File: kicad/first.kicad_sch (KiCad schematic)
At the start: 22 parts, among them J1 Conn_01x04_Pin, P1 USB_C_Plug_USB2.0, SW1 SW_SPDT, U1 STM32F407VETx, Y1 X MHz

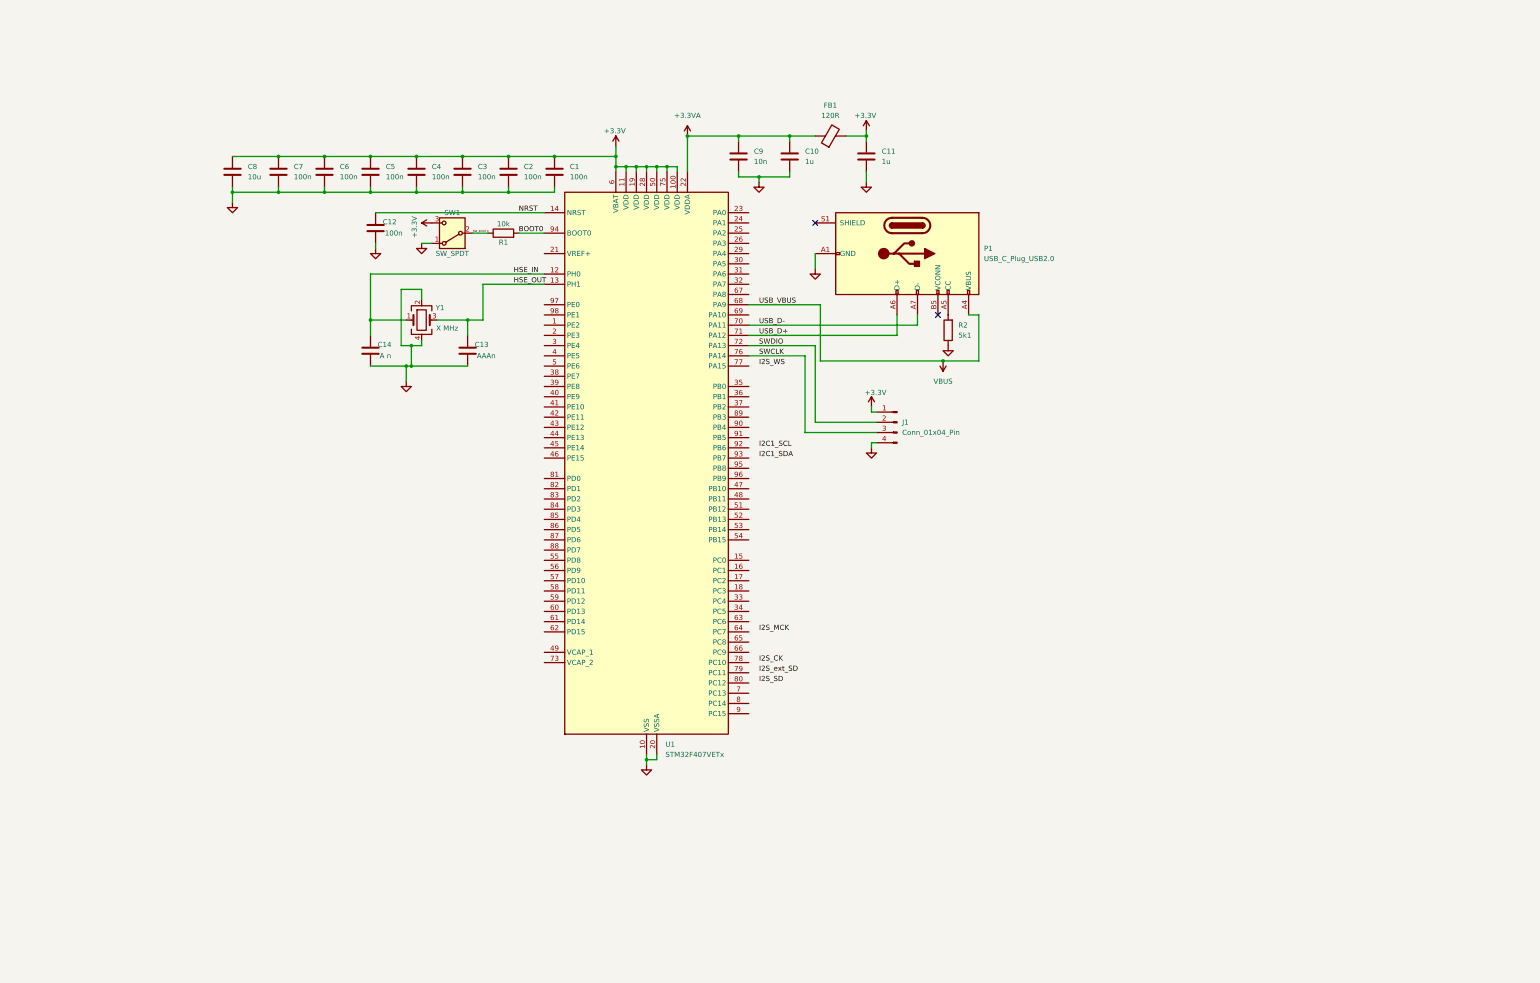
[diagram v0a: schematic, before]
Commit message: added LDO
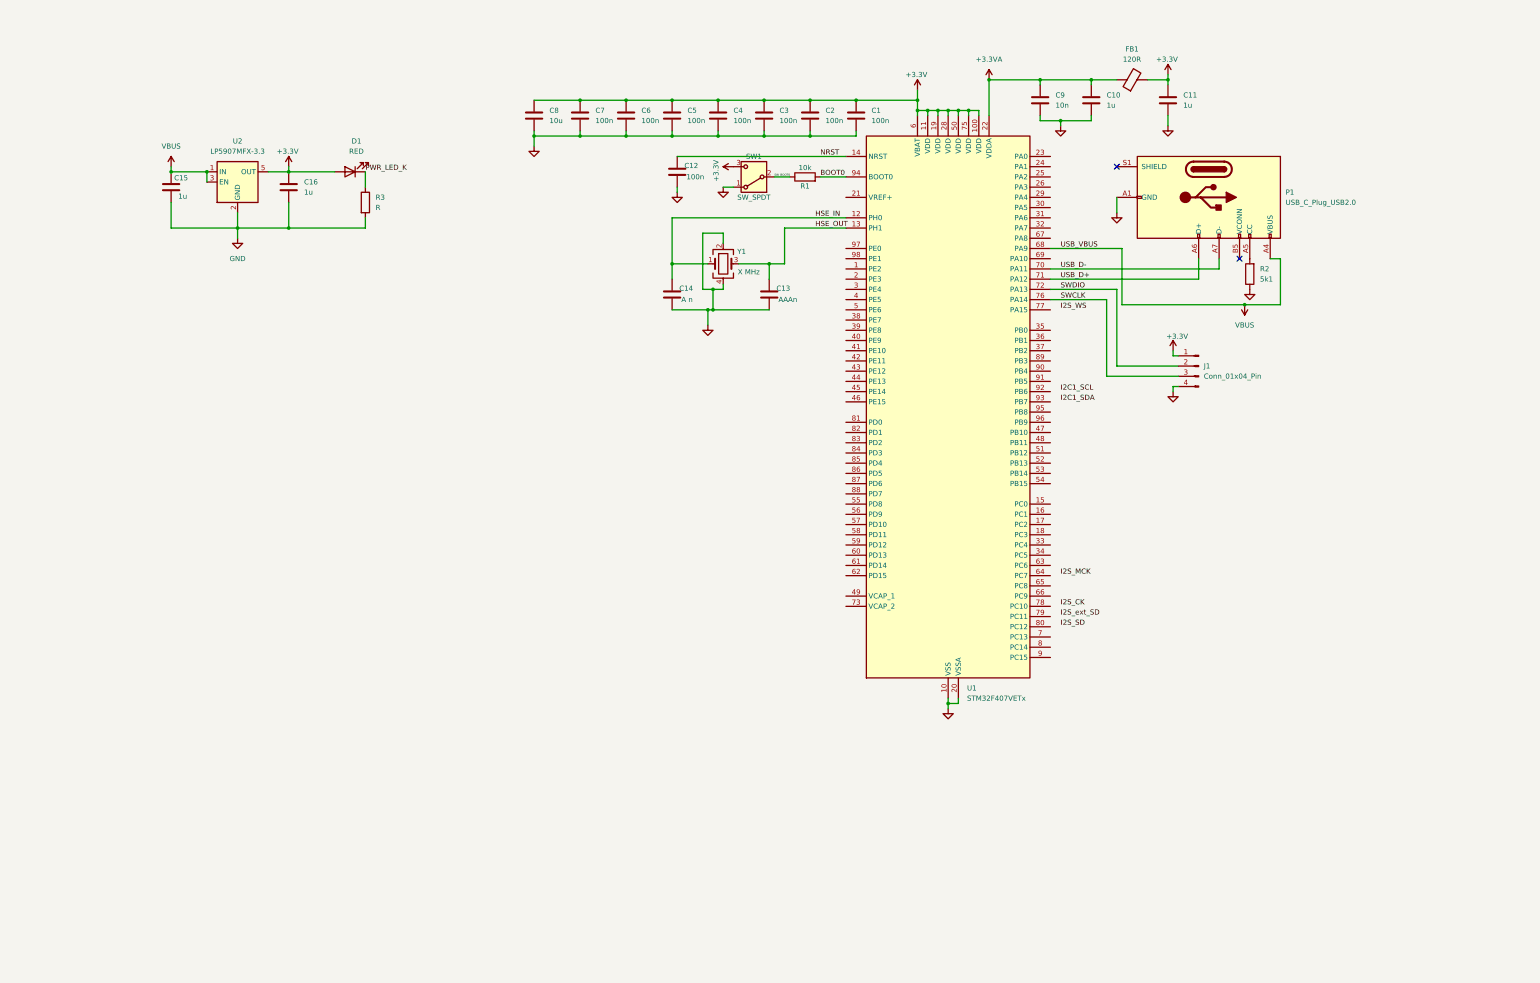
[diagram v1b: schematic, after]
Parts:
- added C15, C16: 1u, symbol Device:C
- added D1: RED, symbol Device:LED
- added R3: R, symbol Device:R
- added U2: LP5907MFX-3.3, Package_TO_SOT_SMD:SOT-23-5, symbol Regulator_Linear:LP5907MFX-3.3
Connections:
- net +3.3V: now also C16.1, D1.2 (A), U2.5 (OUT)
- net GND: now also C15.2, C16.2, R3.2, U2.2 (GND)
- net VBUS: now also C15.1, U2.1 (IN), U2.3 (EN)
- new net PWR_LED_K: D1.1 (K), R3.1
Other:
- moved on the sheet: C1, C10, C11, C12, C13, C14, C2, C3, C4, C5, C6, C7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

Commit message: audio codec + input audio buffers
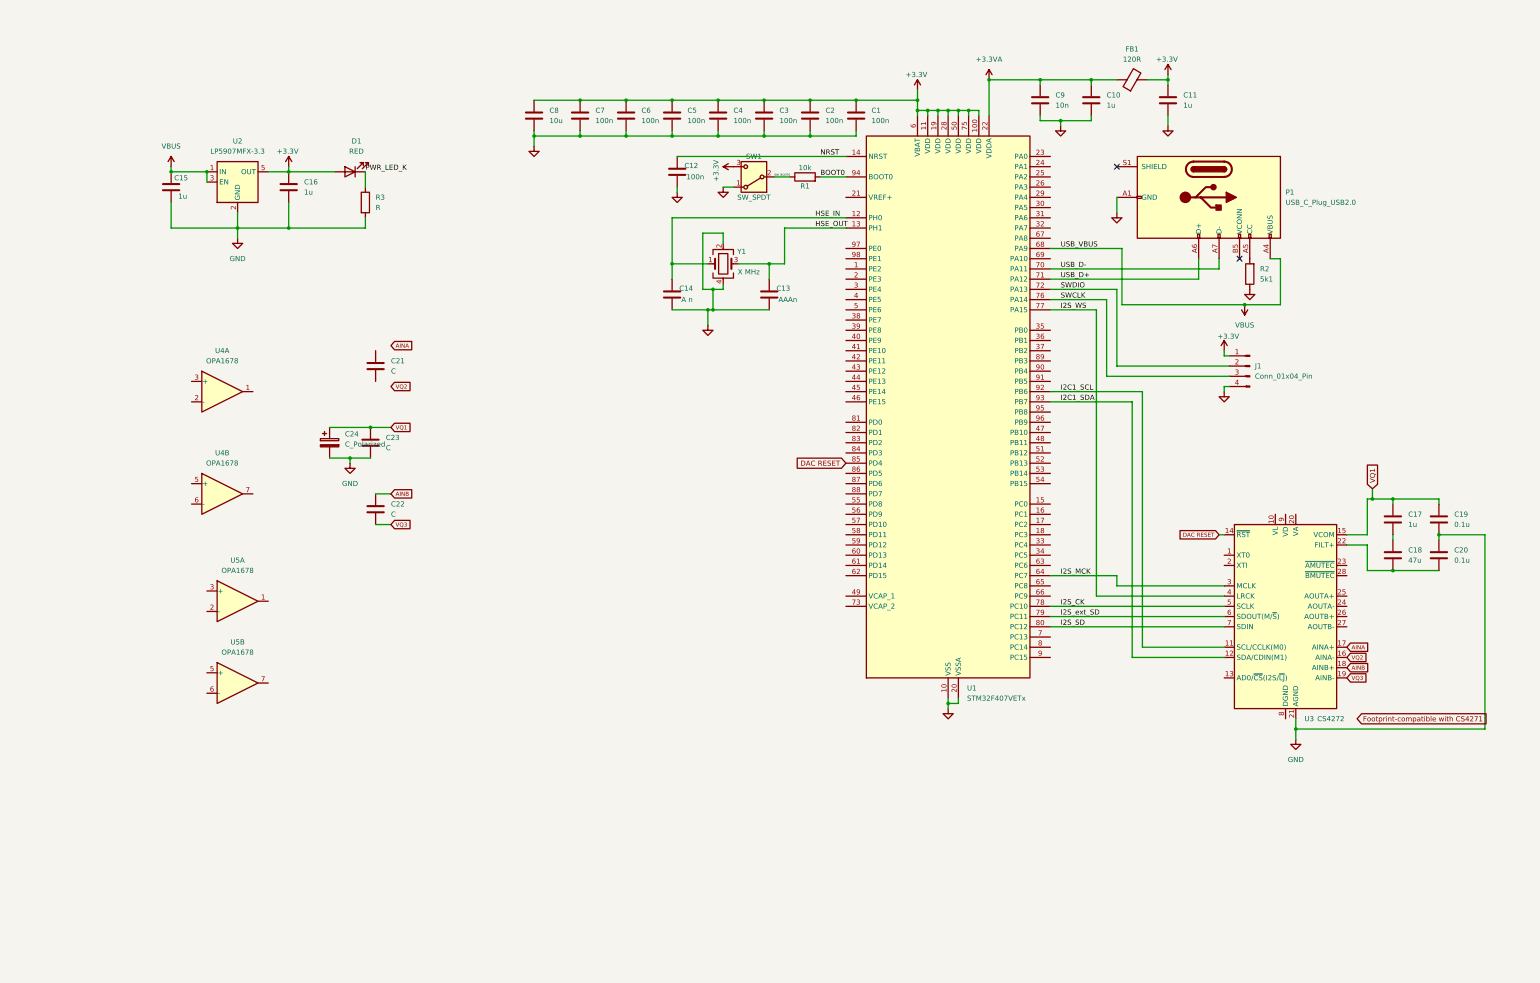
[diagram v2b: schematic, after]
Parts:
- added C17: 1u, symbol Device:C
- added C18: 47u, symbol Device:C
- added C19, C20: 0.1u, symbol Device:C
- added C21, C22, C23: C, symbol Device:C
- added C24: C_Polarized, symbol Device:C_Polarized
- added U3: CS4272, Package_SO:TSSOP-28_4.4x9.7mm_P0.65mm, symbol Audio:CS4272
- added U4, U5: OPA1678, Package_SO:SOIC-8_3.9x4.9mm_P1.27mm, symbol Amplifier_Operational:OPA1678
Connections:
- net GND: now also C19.2, C20.1, C23.2, C24.2, U3.21 (AGND)
- net I2C1_SCL: now also U1.92 (PB6), U3.11 (SCL/CCLK(M0))
- net I2C1_SDA: now also U1.93 (PB7), U3.12 (SDA/CDIN(M1))
- net I2S_CK: now also U1.78 (PC10), U3.5 (SCLK)
- net I2S_MCK: now also U1.64 (PC7), U3.3 (MCLK)
- net I2S_SD: now also U1.80 (PC12), U3.7 (SDIN)
- net I2S_WS: now also U1.77 (PA15), U3.4 (LRCK)
- net I2S_ext_SD: now also U1.79 (PC11), U3.6 (SDOUT(M/~{S}))
- net DAC RESET: now reaches U1.85 (PD4)
- net DAC RESET: now also U3.14 (~{RST})
- new net: C18.2, C20.2, U3.22 (FILT+)
- new net: C17.2, C18.1
- new net AINA: U3.17 (AINA+)
- new net AINB: C22.1, U3.18 (AINB+)
- new net VQ1: C17.1, C19.1, C23.1, C24.1, U3.15 (VCOM)
- new net VQ2: U3.16 (AINA-)
- new net VQ3: C22.2, U3.19 (AINB-)
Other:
- moved on the sheet: J1

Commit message: analog output filters
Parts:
- removed U4, U5: OPA1678, Package_SO:SOIC-8_3.9x4.9mm_P1.27mm, symbol Amplifier_Operational:OPA1678
- added C25, C26: 10u, symbol Device:C_Polarized
- added C27, C28, C32, C38: 470p, symbol Device:C
- added C29, C35: 2200p, symbol Device:C
- added C30, C36: 680p, symbol Device:C
- added C31, C39: 1n5, symbol Device:C
- added C33, C34, C37, C40: 22u, symbol Device:C_Polarized
- added R10, R18: 4k42, symbol Device:R
- added R11, R21: 2k32, symbol Device:R
- added R12, R22: 715, symbol Device:R
- added R13, R19: 1k33, symbol Device:R
- added R14, R20: 1k5, symbol Device:R
- added R15, R24: 560, symbol Device:R
- added R16, R25: 47k, symbol Device:R
- added R17, R23: 4k99, symbol Device:R
- added R4, R5: 10k, symbol Device:R
- added R6, R8: 634, symbol Device:R
- added R7, R9: 91, symbol Device:R
- added U4, U5, U6, U7: NE5532, Package_SO:SOIC-8_5.3x6.2mm_P1.27mm, symbol Amplifier_Operational:NE5532
- C19, C20: value 0.1u -> 100n
- C21, C22: value C -> 2700p
- C23: value C -> 100n
- C24: value C_Polarized -> 1u
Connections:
- net AINA: now also C21.1, R6.2, R7.2
- net AINB: now also C22.2, R8.2, R9.2; no longer C22.1
- net GND: now also C29.2, C30.2, C31.1, C34.2, C35.2, C36.2, C37.2, C39.1, R16.1, R25.1
- net VQ1: now also U5.3 (+)
- net VQ2: now also C21.2, C22.1, U3.19 (AINB-), R4.2, R5.1, U5.1, U5.2 (-)
- net AOUTA-: now reaches U3.24 (AOUTA-)
- net AOUTA-: now also R10.1
- net AOUTA+: now reaches U3.25 (AOUTA+)
- net AOUTA+: now also R13.1
- net AOUTB+: now reaches U3.26 (AOUTB+)
- net AOUTB+: now also R19.1
- net AOUTB-: now reaches U3.27 (AOUTB-)
- net AOUTB-: now also R18.1
- removed net VQ3: C22.2, U3.19 (AINB-)
- new net: C30.1, R12.1, R13.2, R14.1
- new net: C34.1, R14.2
- new net: C29.1, R10.2, R11.1, R17.1
- new net: C35.1, R18.2, R21.1, R23.1
- new net: C40.2, R24.1
- new net: C38.2, R21.2, U7.3 (+)
- new net: C26.1, R5.2, U4.5 (+)
- new net: C28.2, R8.1, U4.6 (-)
- new net: C28.1, R9.1, U4.7
- new net: C31.2, R12.2, U6.2 (-)
- new net: C33.1, U6.1
- new net: C33.2, R15.1
- new net: C27.1, R7.1, U4.1
- new net: C27.2, R6.1, U4.2 (-)
- new net: C25.1, R4.1, U4.3 (+)
- new net: C36.1, R19.2, R20.1, R22.1
- new net: C32.1, R17.2
- new net: C32.2, R11.2, U6.3 (+)
- new net: C39.2, R22.2, U7.2 (-)
- new net: C38.1, R23.2
- new net: C40.1, U7.1
- new net: C37.1, R20.2
- new net AINL: C25.2
- new net AINR: C26.2
- new net AOUTA: R15.2, R16.2
- new net AOUTB: R24.2, R25.2
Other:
- moved on the sheet: C15, C16, C21, C22, C23, C24, D1, R3, U2

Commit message: aaa
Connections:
- net GND: now also U3.2 (XTI), U3.8 (DGND)
- no-connect marks 2 -> 3
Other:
- moved on the sheet: C17, C18, C19, C20

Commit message: working on codec supplies
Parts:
- added C41: 100n, symbol Device:C
- added C42: 1u, symbol Device:C
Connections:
- net +3.3V: now also U3.10 (VL), U3.9 (VD), C41.1, C42.1
- net GND: now also C41.2, C42.2
- net VBUS: now also U3.20 (VA)

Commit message: parts for mute control circuit, need to rethink analog power input
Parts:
- added Q1: MMUN2111LT1G, easyeda2kicad:SOT-23-3_L2.9-W1.3-P1.90-LS2.4-BR, symbol easyeda2kicad:MMUN2111LT1G
- added Q2: MMBT3904, Package_TO_SOT_SMD:SOT-23, symbol Transistor_BJT:MMBT3904
- added R26: 10k, symbol Device:R
- added R27: 2k, symbol Device:R
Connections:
- net GND: now also Q2.2 (E), R26.2
- net AMUTEC: now reaches U3.23 (~{AMUTEC})
- net BMUTEC: now reaches U3.28 (~{BMUTEC})
- new net: Q1.2 (E), R26.1, R27.1
- new net: Q2.1 (B), R27.2
- new net VA: Q1.3 (C)
